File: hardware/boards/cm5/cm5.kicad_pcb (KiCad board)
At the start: 6 copper layers, 75.1 x 102 mm, 84 parts, among them J101 10164227-1001A1RLF, J102 10164227-1001A1RLF, J103 BM04B-SRSS-TB, J201 FH12-24S-0.5SVA(54), J401 1054500101, J501 USB4105-GF-A-120, J601 HR911130A, J701 1-2199230-5, M1 CM5, Q401 2N7002, SW501 SKRTLAE010, U101 SN74AHCT1G125DBVR, U301 LM61480RPHR, U401 HD3SS3220RNHR, U402 AP22652W6-7, U403 TPD4E02B04DQAR, U404 TPD4E02B04DQAR, U405 TPD4E05U06DQAR, U501 TPD4E05U06DQAR, U601 TPD4E02B04DQAR, U602 TPD4E02B04DQAR, U701 AP3441SHE-7B

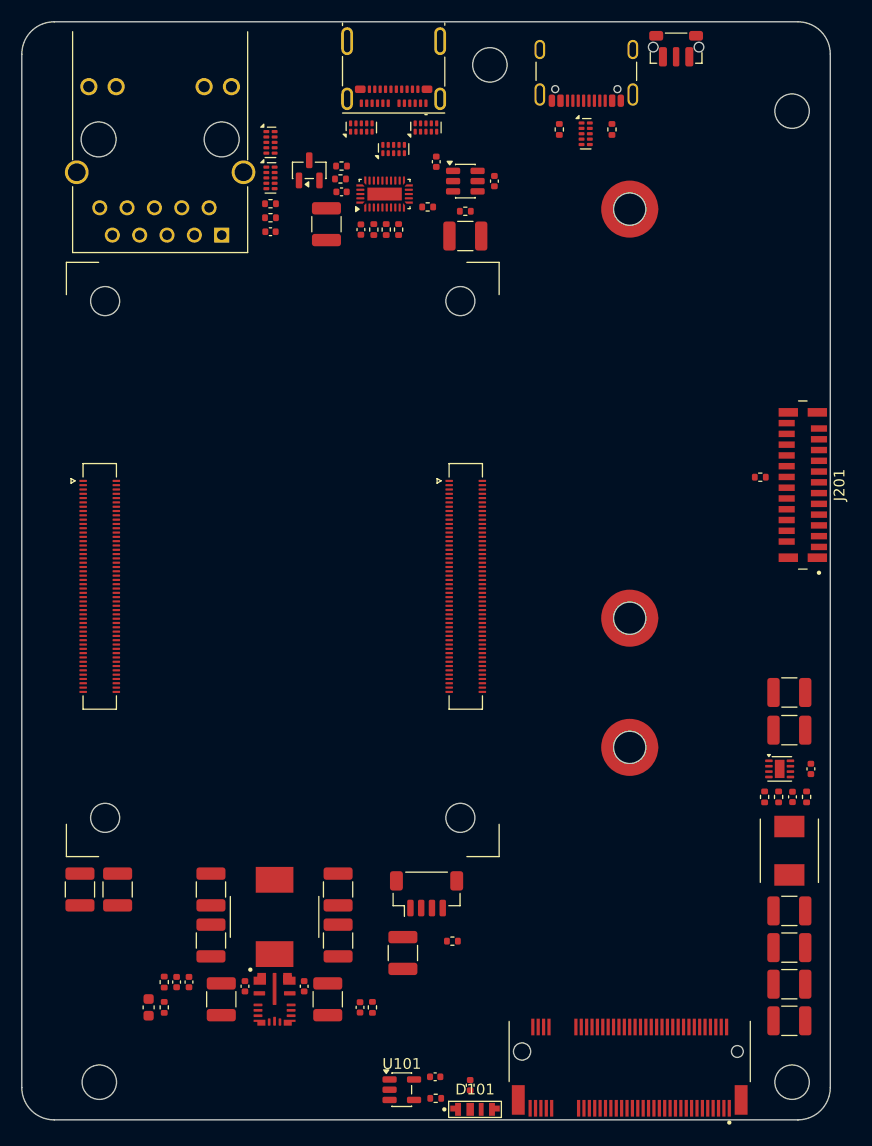
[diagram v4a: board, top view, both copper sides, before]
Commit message: feat(cm5): route the side board
Every net routed and DRC clean with schematic parity. Pairs are length matched; slow lines run as
45-degree diagonals, with In3 carrying the long cross-board runs (RPIBOOT, CM5_3V3, the PCIe
sideband, VBUS_EN) under the outer layers' high-speed walls.

The board is 102 mm deep like the main board, with five mounting holes at the corners and beside
the rear ports. The service port joins its D pins over and under the receptacle's pad row, and
U501's CC channels follow the connector's order so both CC lines run straight to R501 and R502.
The jack LED resistors sit west of the jack, R101 beside the fan header and R406 beside Q401.
The MDI pairs have no ESD array, as on the CM5 IO board. SW501's twin pin-1 pads are marked as
jumpered.
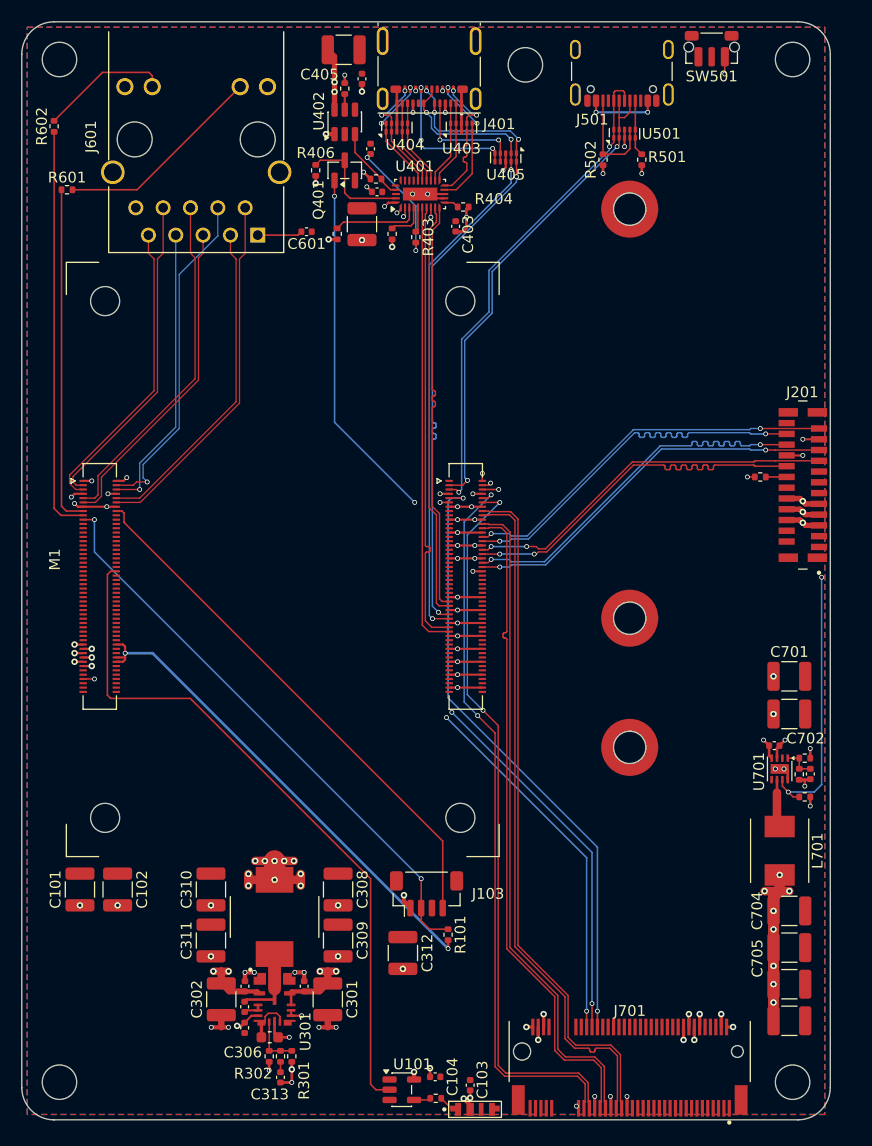
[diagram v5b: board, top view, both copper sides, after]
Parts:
- removed U601, U602: TPD4E02B04DQAR, Package_SON:USON-10_2.5x1.0mm_P0.5mm
- added H5: M3, MountingHole:MountingHole_3.2mm_M3, F.Cu at (103.5, 103.5)
- moved R602 21.8 mm to (103.0, 109.7), turned to -90 degrees
- moved C405 20.7 mm to (129.9, 102.6)
- moved R601 18.9 mm to (104.2, 115.6), turned to 180 degrees
- moved R407 16.0 mm to (130.0, 106.2), turned to 90 degrees
- moved R301 13.7 mm to (125.1, 196.1)
- moved U402 12.5 mm to (130.0, 109.3), turned to 90 degrees
- moved C406 11.9 mm to (132.4, 111.8)
- moved C306 11.6 mm to (123.0, 194.3), turned to 0 degrees
- moved R302 10.8 mm to (123.0, 196.1), turned to -90 degrees
- moved U405 10.4 mm to (144.9, 112.6), turned to -90 degrees
- moved C404 10.3 mm to (131.6, 105.3)
- moved C313 9.84 mm to (124.0, 198.1)
- moved R303 9.68 mm to (124.0, 196.1)
- moved C403 8.81 mm to (140.3, 119.0)
- moved C307 7.62 mm to (120.7, 193.4), turned to -90 degrees
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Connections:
- J102 pad 16: PCIE_RX_P -> PCIE_RX_N
- J102 pad 18: PCIE_RX_N -> PCIE_RX_P
- J102 pad 22: PCIE_TX_P -> PCIE_TX_N
- J102 pad 24: PCIE_TX_N -> PCIE_TX_P
- J102 pad 28: SIDE_TX_N -> SIDE_TX_P
- J102 pad 30: SIDE_TX_P -> SIDE_TX_N
- J102 pad 40: SIDE_RX_N -> SIDE_RX_P
- J102 pad 42: SIDE_RX_P -> SIDE_RX_N
- U501 pad 4: /Service port/CC1 -> /Service port/CC2
- U501 pad 5: /Service port/CC2 -> /Service port/CC1
- U501 pad 6: /Service port/CC2 -> /Service port/CC1
- U501 pad 7: /Service port/CC1 -> /Service port/CC2
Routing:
- net CM5_3V3: track 0.00 -> 181.8 mm, vias 0 -> 4
- net SIDE_BUS: track 0.00 -> 99.2 mm, vias 0 -> 7
- net GND: track 0.00 -> 90.9 mm, vias 0 -> 55
- net RPIBOOT_N: track 0.00 -> 84.5 mm, vias 0 -> 2
- net VBUS_EN: track 0.00 -> 73.1 mm, vias 0 -> 4
- net PCIE_CLK_N: track 0.00 -> 67.8 mm, vias 0 -> 2
- net PCIE_CLK_P: track 0.00 -> 67.6 mm, vias 0 -> 2
- net /Compute module/LED_DATA: track 0.00 -> 64.7 mm
- net PCIE_PWR_EN: track 0.00 -> 64.5 mm, vias 0 -> 3
- net PCIE_RX_N: track 0.00 -> 64.3 mm
- net PCIE_RX_P: track 0.00 -> 64.3 mm
- net PCIE_WAKE_N: track 0.00 -> 63.4 mm, vias 0 -> 3
- net ACC_D_P: track 0.00 -> 62.2 mm, vias 0 -> 5
- net PCIE_TX_N: track 0.00 -> 61.7 mm
- net PCIE_TX_P: track 0.00 -> 61.7 mm
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- added copper zone on In2.Cu, net 5V
- added copper zone on B.Cu, net GND
- added copper zone on F.Cu, net GND
- added copper zone on In1.Cu, net GND
- added copper zone on In4.Cu, net GND
- added copper zone on In3.Cu, net NVME_3V3

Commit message: fix(cm5): centre the board on its sheet
The outline's centre sits on the A4 page's centre instead of running off the drawing frame. D101
shares C103's 5 V via instead of having its own, on a 0.25 mm stub in place of the netclass's 0.4.
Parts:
- moved C701 47.3 mm to (182.3, 114.8)
- moved C702 47.3 mm to (182.3, 118.3)
- moved C703 47.3 mm to (180.9, 121.2)
- moved J501 47.3 mm to (166.7, 57.6)
- moved C101 47.3 mm to (116.4, 134.6)
- moved C102 47.3 mm to (119.9, 134.6)
- moved C103 47.3 mm to (152.7, 152.8)
- moved C104 47.3 mm to (149.4, 152.0)
- moved C301 47.3 mm to (139.4, 144.8)
- moved C302 47.3 mm to (129.5, 144.8)
- moved C303 47.3 mm to (137.2, 143.6)
- moved C304 47.3 mm to (131.7, 143.6)
- moved C305 47.3 mm to (131.7, 145.5)
- moved C306 47.3 mm to (134.0, 148.3)
- moved C307 47.3 mm to (131.7, 147.4)
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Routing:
- net 5V: track 35.9 -> 35.7 mm, vias 43 -> 42

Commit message: feat(cm5): label the side board's silkscreen
The back carries the main board's identity block: iasis CM5, the revision and the repository. The front names the accessory and service USB-C ports, the RPIBOOT button, the fan header, the main board link at J201 and the 2230, 2242 and 2280 standoffs.
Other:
- board text added: "2230"
- board text added: "2242"
- board text added: "2280"
- board text added: "ACCESSORY"
- board text added: "FAN"
- board text added: "MAIN"
- board text added: "REV ${REVISION}"
- board text added: "RPIBOOT"
- board text added: "SERVICE"
- board text added: "github.com/hydazz/iasis"
- board text added: "iasis CM5"
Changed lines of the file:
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@@
 		(descr "Bourns SRP5030CC shielded inductor, 5.7x5.2mm; manufacturer recommended 6.5x2.8mm land envelope")
 		(property "Reference" "L701"
-			(at 0 -3.519999 90)
+			(at 0 3.52 90)
 			(layer "F.SilkS")
 			(effects
@@
 			(at 0 -2.719999 0)
 			(layer "F.SilkS")
+			(hide yes)
 			(effects
 				(font
@@
 		(tags "Texas WQFN NoLead")
 		(property "Reference" "U401"
-			(at 2.573515 -0.5 0)
+			(at 2.573515 0 0)
 			(layer "F.SilkS")
 			(effects
@@
 		(tags "resistor")
 		(property "Reference" "R201"
-			(at 0 -1.17 0)
+			(at -0.25 -1.49 0)
 			(layer "F.SilkS")
-			(hide yes)
 			(effects
 				(font
@@
 		(tags "connector JST SH vertical")
 		(property "Reference" "J103"
-			(at 5.712136 0 0)
+			(at 4.5 3.269999 0)
 			(layer "F.SilkS")
 			(effects
@@
 		(tags "capacitor")
 		(property "Reference" "C705"
-			(at -2.97 1 90)
+			(at -4.208095 0 0)
 			(layer "F.SilkS")
 			(effects
@@
 			(at -1.953515 -0.000001 0)
 			(layer "F.SilkS")
+			(hide yes)
 			(effects
 				(font
@@
 		(tags "resistor")
 		(property "Reference" "R502"
-			(at 0 1.14 90)
+			(at 0.25 1.14 90)
 			(layer "F.SilkS")
 			(effects
@@
 		(tags "resistor")
 		(property "Reference" "R101"
-			(at 0 1.139999 90)
+			(at -0.25 -1.14 90)
 			(layer "F.SilkS")
 			(effects
@@
 		(tags "capacitor")
 		(property "Reference" "C704"
-			(at -2.993515 0 90)
+			(at -4.231184 0 0)
 			(layer "F.SilkS")
 			(effects
@@
 		(tags "capacitor")
 		(property "Reference" "C312"
-			(at 0 2.269999 90)
+			(at -2.969999 -0.000001 0)
 			(layer "F.SilkS")
 			(effects
@@
 		(tags "capacitor")
 		(property "Reference" "C706"
-			(at 0 -2.3 0)
+			(at -4.208095 -0.000001 0)
 			(layer "F.SilkS")
-			(hide yes)
 			(effects
 				(font
@@
 			(at -1.603515 0.749999 0)
 			(layer "F.SilkS")
+			(hide yes)
 			(effects
 				(font
@@
 		(tags "USB C Type-C Receptacle SMD USB 2.0 16P 16C USB4105-15-A USB4105-15-A-060 USB4105-15-A-120 USB4105-GF-A USB4105-GF-A-060 USB4105-GF-A-120")
 		(property "Reference" "J501"
-			(at 2.75 -5.429999 0)
+			(at -7.131415 -4.29 0)
 			(unlocked yes)
 			(layer "F.SilkS")
@@
 		(tags "capacitor")
 		(property "Reference" "C703"
-			(at 0 -1.16 180)
+			(at 2.818095 0.75 0)
 			(layer "F.SilkS")
-			(hide yes)
 			(effects
 				(font
@@
 		(layer "Edge.Cuts")
 	)
+	(gr_text "ACCESSORY"
+		(at 148.84 65.55 0)
+		(layer "F.SilkS")
+		(effects
+			(font
+				(size 1 1)
+				(thickness 0.15)
+			)
+		)
+	)
+	(gr_text "SERVICE"
+		(at 162.74 63.079999 0)
+		(layer "F.SilkS")
+		(effects
+			(font
+				(size 1 1)
+				(thickness 0.15)
+			)
+		)
+	)
+	(gr_text "2280"
+		(at 167.468728 74.971268 0)
+		(layer "F.SilkS")
+		(effects
+			(font
+				(size 1 1)
+				(thickness 0.15)
+			)
+		)
+	)
+	(gr_text "2242"
+		(at 167.468728 112.994784 0)
+		(layer "F.SilkS")
+		(effects
+			(font
+				(size 1 1)
+				(thickness 0.15)
+			)
+		)
+	)
+	(gr_text "2230"
+		(at 167.468728 124.971268 0)
+		(layer "F.SilkS")
+		(effects
+			(font
+				(size 1 1)
+				(thickness 0.15)
+			)
+		)
+	)
+	(gr_text "RPIBOOT"
+		(at 175.079999 59.069999 0)
+		(layer "F.SilkS")
+		(effects
+			(font
+				(size 1 1)
+				(thickness 0.15)
+			)
+		)
+	)
+	(gr_text "MAIN"
+		(at 180.220208 98.78 90)
+		(layer "F.SilkS")
+		(effects
+			(font
+				(size 1.1 1.1)
+				(thickness 0.17)
+			)
+		)
+	)
+	(gr_text "FAN"
+		(at 154.056427 135 0)
+		(layer "F.SilkS")
+		(effects
+			(font
+				(size 1.2 1.2)
+				(thickness 0.18)
+			)
+		)
+	)
+	(gr_text "github.com/hydazz/iasis"
+		(at 183 83.699999 0)
+		(layer "B.SilkS")
+		(effects
+			(font
+				(size 1 1)
+				(thickness 0.18)
+			)
+			(justify left top mirror)
+		)
+	)
+	(gr_text "REV ${REVISION}"
+		(at 164.983332 80.2 0)
+		(layer "B.SilkS")
+		(effects
+			(font
+				(size 1.2 1.2)
+				(thickness 0.2)
+			)
+			(justify left top mirror)
+		)
+	)
+	(gr_text "iasis CM5"
+		(at 183 79.5 0)
+		(layer "B.SilkS")
+		(effects
+			(font
+				(size 2 2)
+				(thickness 0.25)
+			)
+			(justify left top mirror)
+		)
+	)
 	(segment

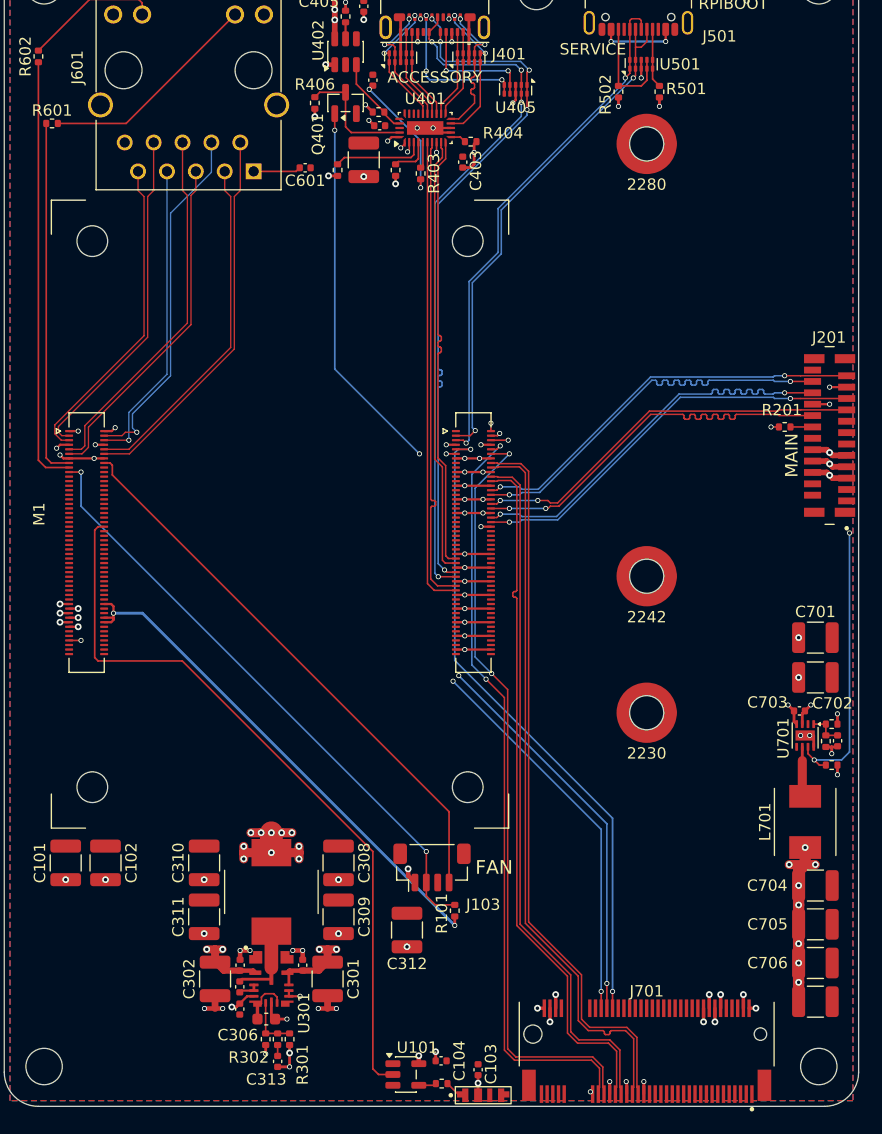
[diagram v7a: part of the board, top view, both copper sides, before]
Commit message: fix(cm5): straighten PCIE_PWR_EN and tidy the side board's vias
PCIE_PWR_EN runs diagonally from J102 to U701 on F.Cu, In3 and B.Cu: 44 mm against 65 mm along
the board edge, with a ring of clearance around spacer H703's hole. The vias of VBUS_EN, ACC_VBUS,
SIDE_BUS, PCIE_CLKREQ_N, PCIE_RST_N, CC1, CC2, CM5_3V3 and FAN_PWM sit where their tracks turn
instead of past the bend or below their pads, and duplicate stubs on the CC and regulator nets are
gone. The USB and Ethernet pairs are unchanged. DRC, schematic parity and ERC pass.
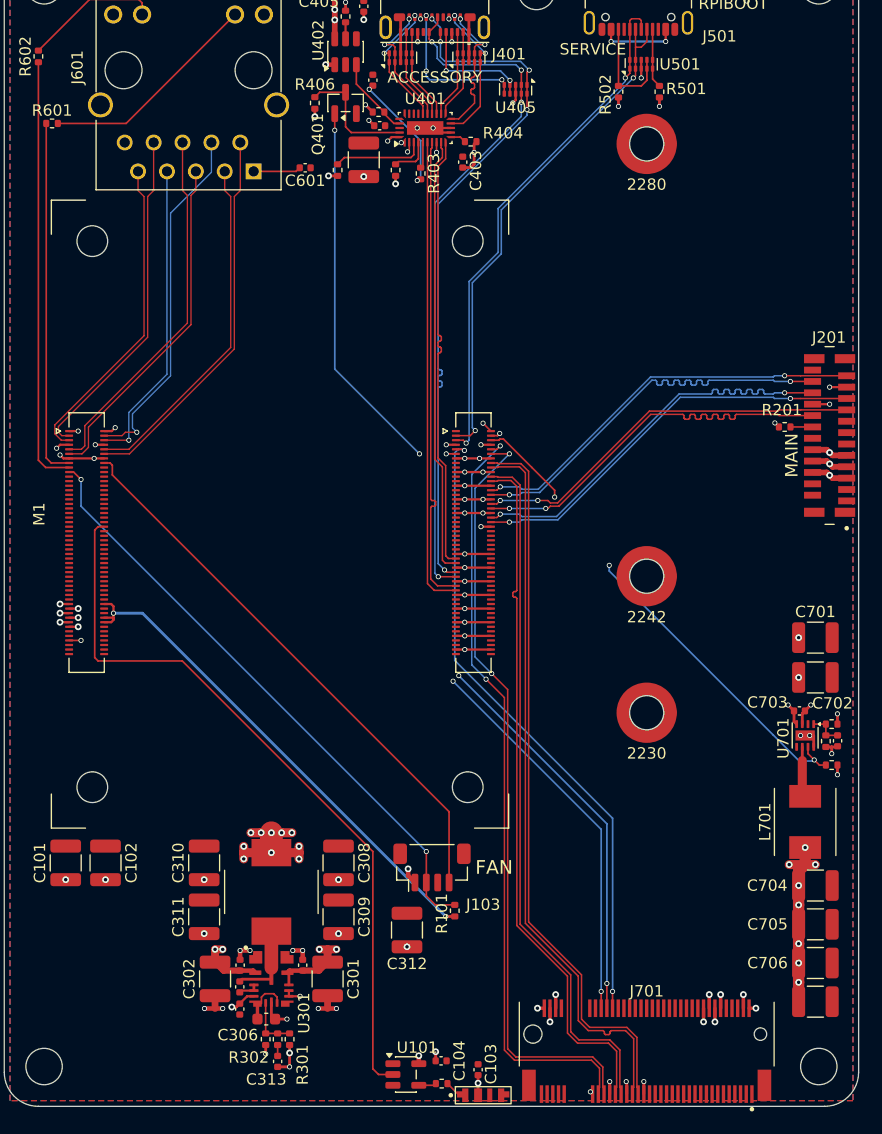
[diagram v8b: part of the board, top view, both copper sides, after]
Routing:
- net PCIE_PWR_EN: track 64.5 -> 44.0 mm
- net SIDE_BUS: track 99.2 -> 97.4 mm
- net /Accessory port/CC2: track 21.8 -> 20.1 mm
- net PCIE_RST_N: track 57.4 -> 56.1 mm
- net CM5_3V3: track 181.8 -> 180.7 mm
- net /Accessory port/CC1: track 20.4 -> 19.4 mm
- net VBUS_EN: track 73.1 -> 72.2 mm
- net ACC_VBUS: track 41.6 -> 40.7 mm
